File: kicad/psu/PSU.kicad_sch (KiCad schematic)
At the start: 57 parts, among them J1 B2B-PH-K-S, J2 5015680407, J3 UJ20-C-H-G-SMT-1-P16-TR, J4 5015680407, U1 BQ21040DBVR, U2 RT4812GJ8F, U3 AP3445LW6-7, U4 AP3445LW6-7, U5 LM66200DRLR

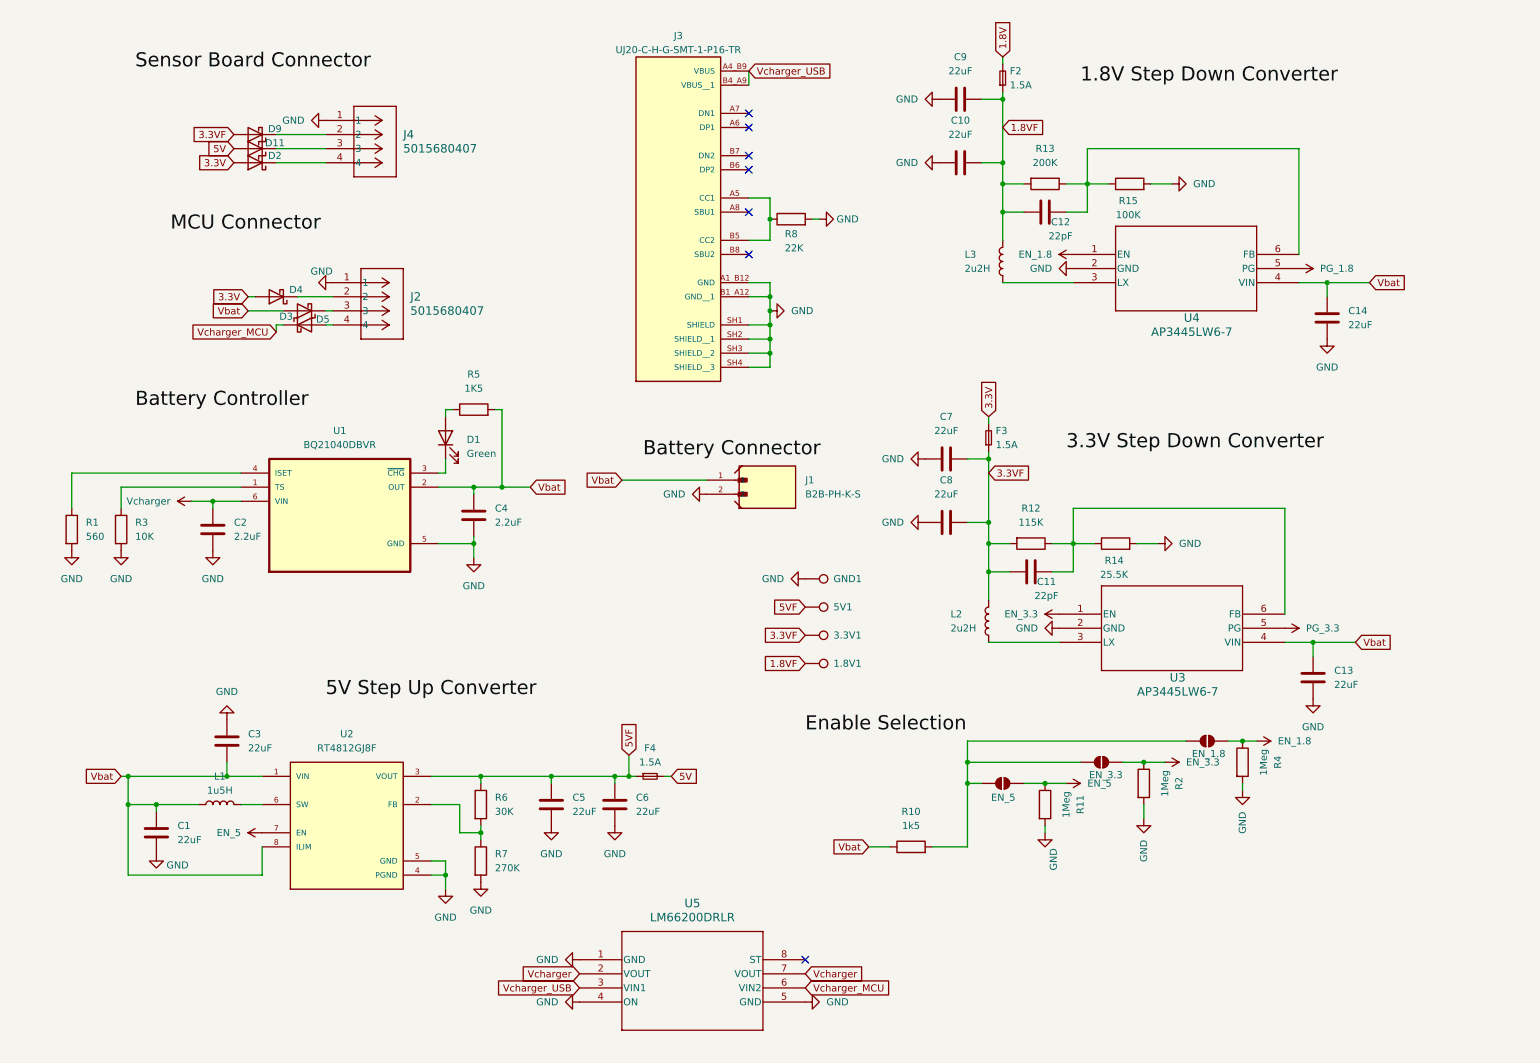
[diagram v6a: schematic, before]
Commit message: feat: schematic for psu
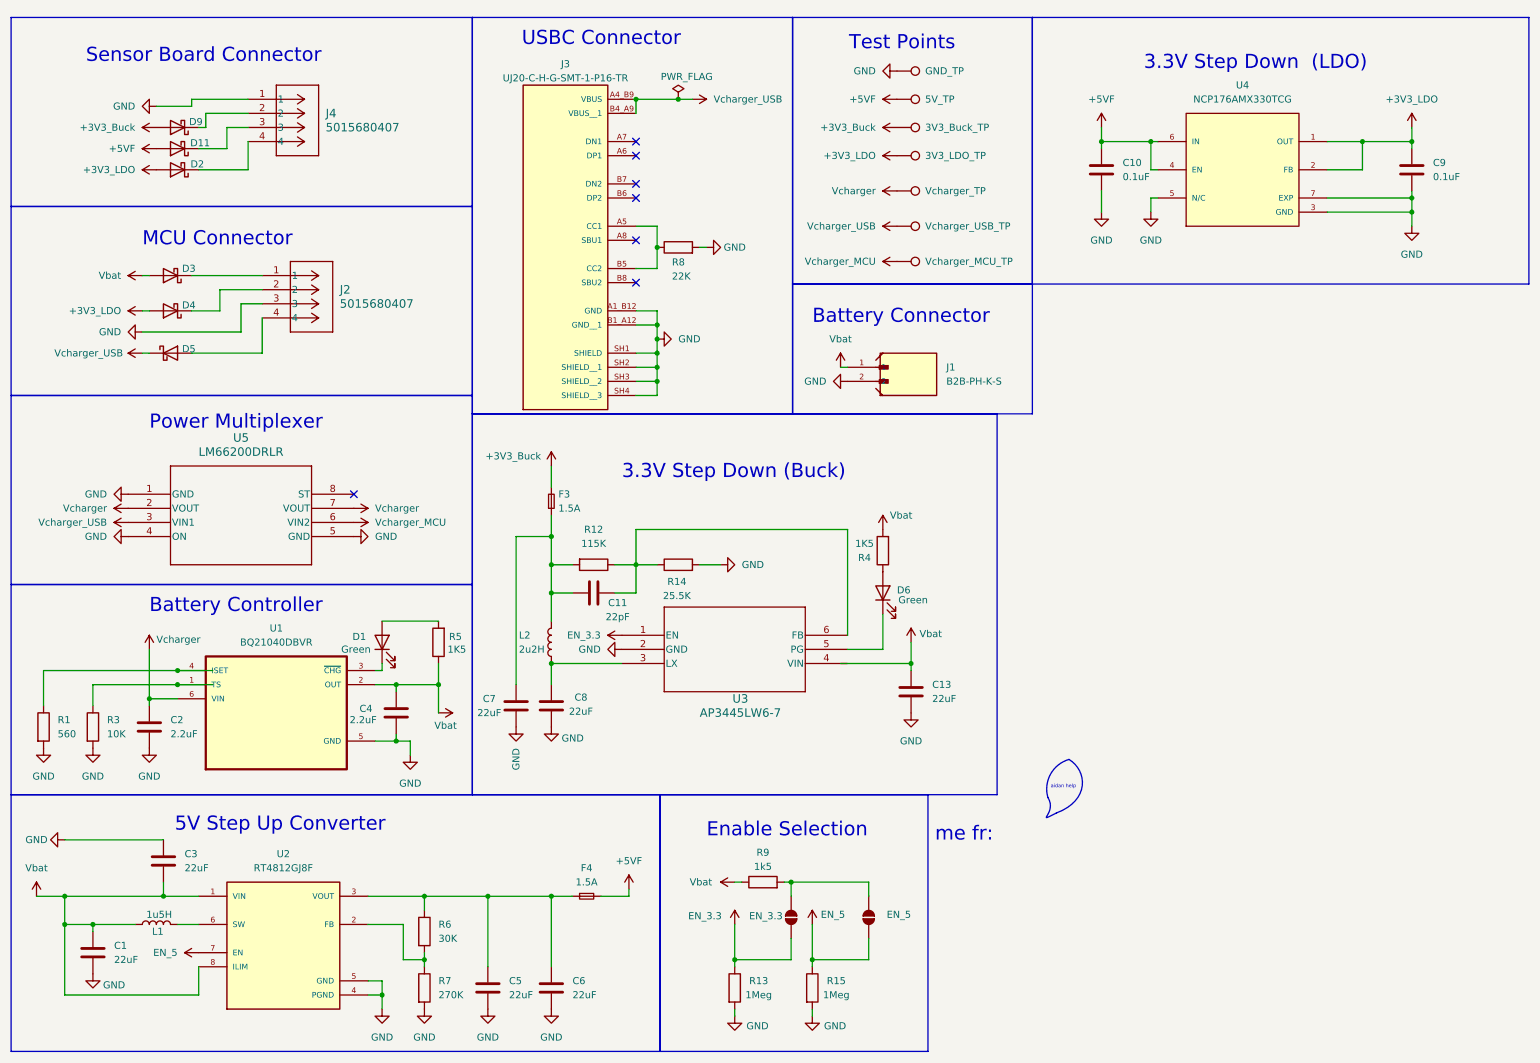
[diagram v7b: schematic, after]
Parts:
- removed 1.8V1: TestPoint, TestPoint:TestPoint_Pad_1.5x1.5mm, symbol Connector:TestPoint
- removed C12: 22pF, Capacitor_SMD:C_0805_2012Metric, symbol Device:C
- removed C14: 22uF, Capacitor_SMD:C_0805_2012Metric, symbol Device:C
- removed EN_1.8: EN_1.8, Jumper:SolderJumper-2_P1.3mm_Open_Pad1.0x1.5mm, symbol Jumper:SolderJumper_2_Open
- removed F2: 1.5A, Fuses:0451Series_LTF, symbol Device:Fuse_Small
- removed L3: 2u2H, Inductor_SMD:L_1210_3225Metric, symbol Device:L
- removed R10: 1k5, Resistor_SMD:R_0805_2012Metric, symbol Device:R
- removed R11, R2: 1Meg, Resistor_SMD:R_0805_2012Metric, symbol Device:R
- removed U4: AP3445LW6-7, PSAT_Library:SOT26_AP3445_DIO-L, symbol 2025-11-28_22-50-25:AP3445LW6-7
- added 3V3_LDO_TP, Vcharger_MCU_TP, Vcharger_TP, Vcharger_USB_TP: TestPoint, TestPoint:TestPoint_Pad_1.5x1.5mm, symbol Connector:TestPoint
- added D6: Green, LED_SMD:LED_0805_2012Metric, symbol Device:LED
- added R9: 1k5, Resistor_SMD:R_0805_2012Metric, symbol Device:R
- added U4: NCP176AMX330TCG, NCP176AMX330TCG:PSON40P120X120X45-7N_NCP176AMX330TCG, symbol NCP176AMX330TCG:NCP176AMX330TCG
- C10, C9: value 22uF -> 0.1uF; footprint Capacitor_SMD:C_0805_2012Metric -> (none)
- EN_3.3: value EN_3.3 -> EN_5
- L1: footprint PSAT_Library:IND_SPM6530T-1R5M100 -> Inductor_SMD:L_0805_2012Metric
- R13: value 200K -> 1Meg
- R15: value 100K -> 1Meg
- R4: value 1Meg -> 1K5
- renumbered 3.3V1 to 3V3_Buck_TP, 5V1 to 5V_TP, GND1 to GND_TP
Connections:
- net 1.8VF is gone; now on net GND: C10.2, C9.2, R13.2
- net EN_3.3: now also R13.1
- net EN_5: now also R15.1
- net GND: now also J2.3, U4.3 (GND), U4.5 (N/C), U4.7 (EXP); no longer C10.1, C9.1, J2.1, R4.2
- net Vbat: now also R4.2, R5.1, R9.1; no longer R5.2, U3.4 (VIN)
- net Vcharger: now also Vcharger_TP.1
- net Vcharger_MCU: now also Vcharger_MCU_TP.1; no longer D5.1 (K)
- net Vcharger_USB: now also D5.1 (K), Vcharger_USB_TP.1
- net at EN_3.3.2 (B), EN_5.2 (B): now also R9.2
- net at D1.2 (A): now also R5.2; no longer R5.1
- net at L2.2, U3.3 (LX): now also C8.2
- net at D3.1 (K): now also J2.1; no longer J2.3
- net 3.3V renamed +3V3_LDO
- net +3V3_LDO: now also C9.1, 3V3_LDO_TP.1, U4.1 (OUT), U4.2 (FB); no longer F3.2
- net 3.3VF: no longer names the net of C11.1, C7.2, F3.1, L2.1, R12.2
- net 3.3VF: no longer 3V3_Buck_TP.1, C8.2, D9.2 (A)
- net 5V renamed +5VF
- net +5VF: now also 5V_TP.1, C10.1, U4.4 (EN), U4.6 (IN)
- net 5VF: no longer names the net of C5.2, C6.1, F4.1, R6.1, U2.3 (VOUT)
- net 5VF: no longer 5V_TP.1
- net EN_1.8: no longer names the net of R4.1
- net EN_1.8: now also D6.2 (A)
- net PG_3.3: no longer names the net of U3.5 (PG)
- net PG_3.3: now also D6.1 (K)
- new net +3V3_Buck: 3V3_Buck_TP.1, D9.2 (A), F3.2
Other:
- note added: "3.3V Step Down (Buck)"
- note added: "3.3V Step Down (LDO)"
- note added: "5V Step Up Converter"
- note added: "Battery Connector"
- note added: "Battery Controller"
- note added: "Enable Selection"
- note added: "MCU Connector"
- note added: "Power Multiplexer"
- note added: "Sensor Board Connector"
- note added: "Test Points"
- note added: "USBC Connector"
- note added: "aidan help"
- note added: "me fr:"
- title: (none) -> Power Supply PCB
- moved on the sheet: 3V3_Buck_TP, 5V_TP, C1, C11, C13, C2, C3, C4, C5, C6, C7, C8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

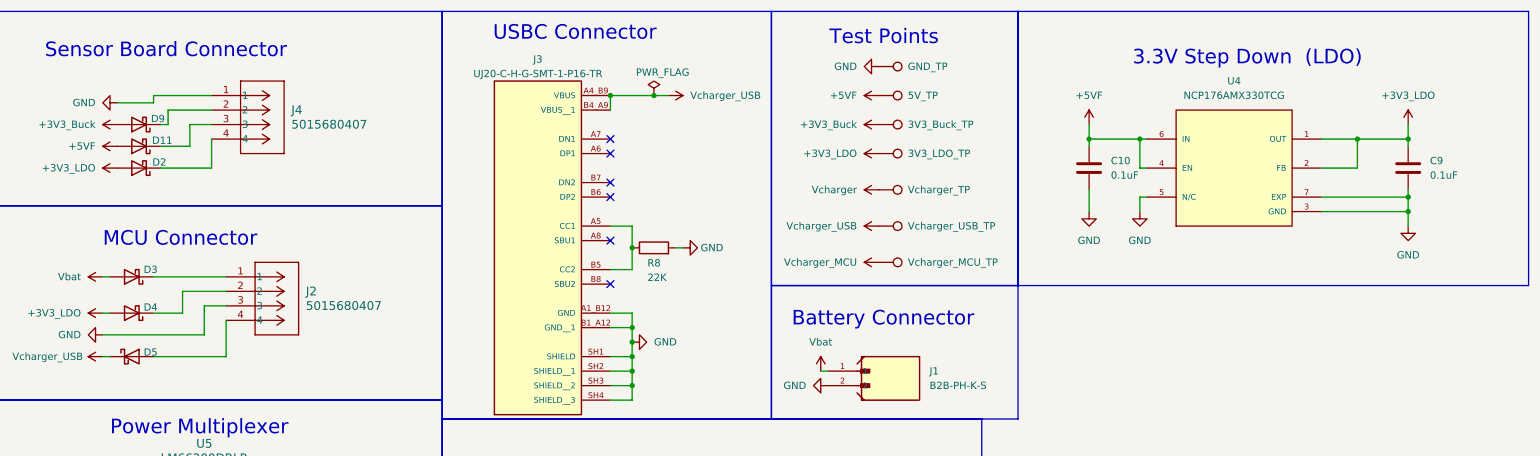
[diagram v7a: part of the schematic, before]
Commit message: feat: complete psu schematic (not sure about the 2 extra pins on the headers though)
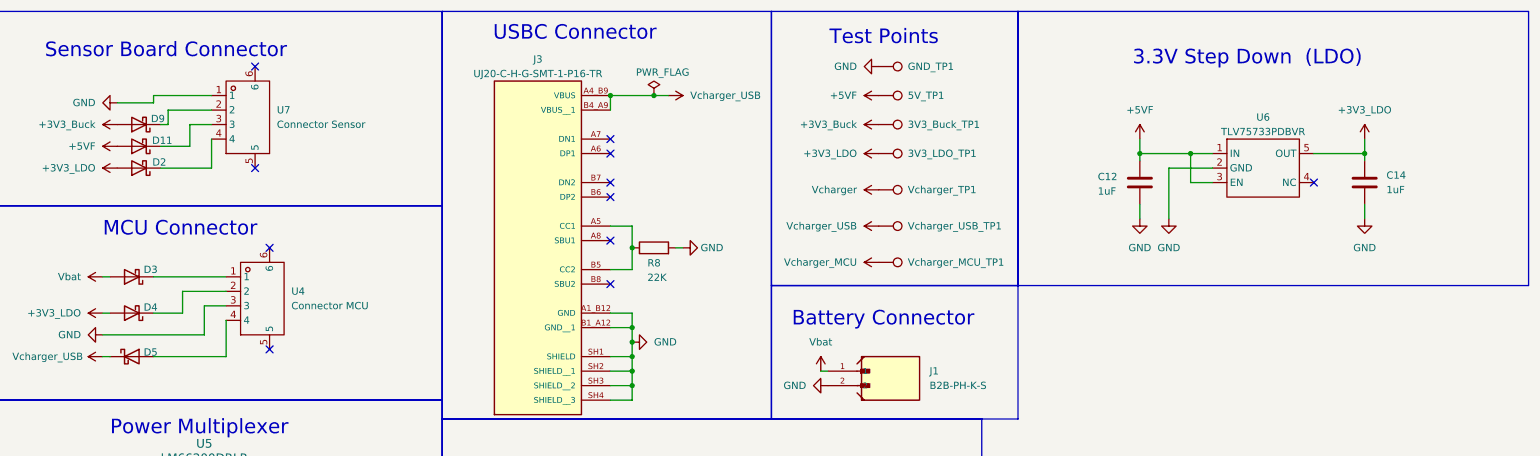
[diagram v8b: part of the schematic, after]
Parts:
- removed C10, C9: 0.1uF, symbol Device:C
- removed J2, J4: 5015680407, CONN_5015680000-SD_04_MOL, symbol 2026-01-26_05-30-52:5015680407
- removed U4: NCP176AMX330TCG, NCP176AMX330TCG:PSON40P120X120X45-7N_NCP176AMX330TCG, symbol NCP176AMX330TCG:NCP176AMX330TCG
- added C12, C14: 1uF, symbol Device:C
- added U4: Connector MCU, ProLib_pcs_2026-01-27:CONN-SMD_4P-P1.25-MX1.25-4P-WT, symbol PSAT_Library:ZX-MX1.25-4PWT
- added U6: TLV75733PDBVR, TLV75733PDBVR:SOT-23-5_L2.9-W1.6-P0.95-LS2.8-BL, symbol PSAT_Library:TLV75733PDBVR
- added U7: Connector Sensor, ProLib_pcs_2026-01-27:CONN-SMD_4P-P1.25-MX1.25-4P-WT, symbol PSAT_Library:ZX-MX1.25-4PWT
- renumbered 3V3_Buck_TP to 3V3_Buck_TP1, 3V3_LDO_TP to 3V3_LDO_TP1, 5V_TP to 5V_TP1, GND_TP to GND_TP1, Vcharger_MCU_TP to Vcharger_MCU_TP1, Vcharger_TP to Vcharger_TP1, Vcharger_USB_TP to Vcharger_USB_TP1
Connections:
- net +3V3_LDO: now also C14.1, U6.5 (OUT)
- net +5VF: now also C12.1, U6.1 (IN), U6.3 (EN)
- net GND: now also C12.2, C14.2, U4.3, U6.2 (GND), U7.1
- net at D4.1 (K): now also U4.2
- net at D2.1 (K): now also U7.4
- net at D9.1 (K): now also U7.2
- net at D11.1 (K): now also U7.3
- net at D3.1 (K): now also U4.1
- net at D5.2 (A): now also U4.4
- no-connect marks 7 -> 12
